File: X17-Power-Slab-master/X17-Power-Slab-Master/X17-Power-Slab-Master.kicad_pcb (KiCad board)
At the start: 2 copper layers, 302.3 x 119 mm, 29 parts, among them J2 ET60T-D04-3-08-D04-X-R1-S, J3 796636-6, Q2 TSM340N06CP ROG

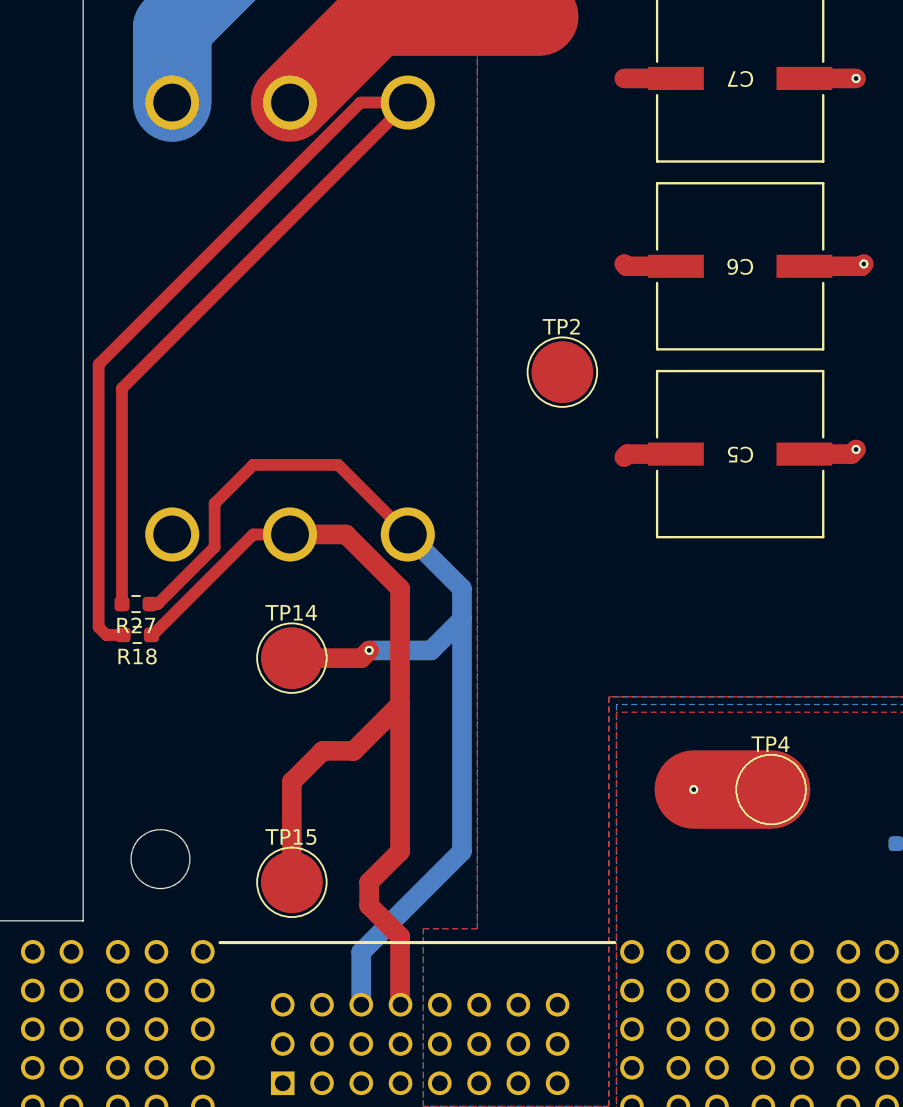
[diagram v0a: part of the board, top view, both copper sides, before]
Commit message: Connector pins renamed and attempt @ fixing airwires for 5V Brick
Still don't understand why the airwire from 5V to 12V_5V_GND test point exists, I also now have airwires across all my P08_1 pins despite the same set up existing for 12V.
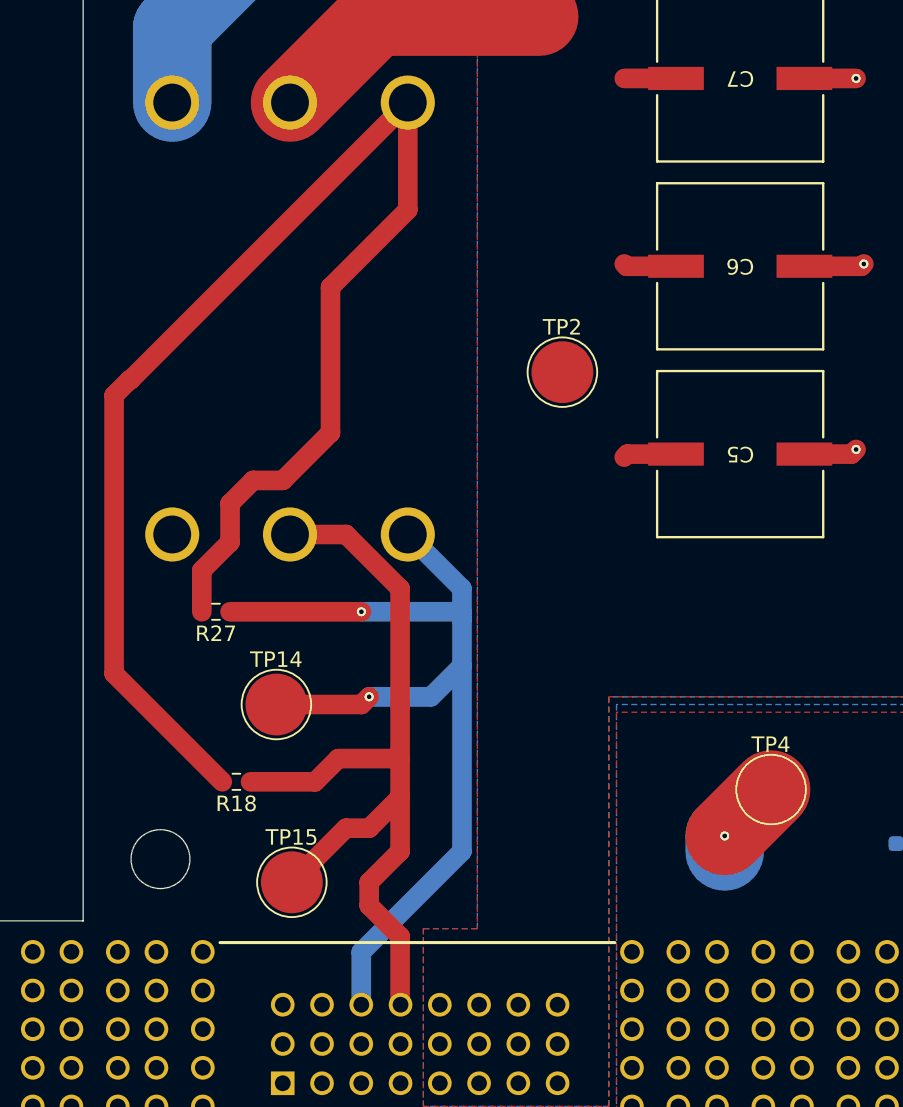
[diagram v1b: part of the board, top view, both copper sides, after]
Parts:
- moved R18 11.5 mm to (81.4, 118.5)
- moved R27 5.19 mm to (80.1, 107.5)
- moved TP14 3.16 mm to (84.0, 113.5)
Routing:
- net Net-(U5-Trim): track 85.9 -> 94.3 mm
- net 5V: track 71.0 -> 63.1 mm, vias 1 -> 2
- net 12V_5V_GND: track 69.4 -> 62.0 mm

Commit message: Minor Edits
Some layout edits, got rid of stm, not done yet
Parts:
- removed the H1 at (-129.8, 147.6)
- removed the H3 at (-7.44, 147.6)
- removed the H4 at (-8.83, 37.2)
- removed TP1, TP4: TestPoint, TestPoint:TestPoint_Pad_D4.0mm
- moved R18 37.1 mm to (89.4, 82.3), turned to 90 degrees
- moved TP2 32.3 mm to (100.6, 124.2)
- moved R27 28.1 mm to (92.5, 82.3), turned to 90 degrees
- moved TP3 7.91 mm to (152.0, 138.0)
- moved TP14 4.61 mm to (88.2, 111.5)
- moved TP15 3.16 mm to (88.0, 124.0), turned to 180 degrees
- moved TP6 2.32 mm to (110.8, 59.5)
- moved R1 1.91 mm to (126.0, 55.0), turned to 180 degrees
- moved TP5 1.80 mm to (77.0, 58.0)
- moved R10 0.75 mm to (125.0, 123.2)
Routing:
- net Net-(U5-Trim): track 94.3 -> 9.93 mm
- net 48V: track 65.5 -> 24.3 mm
- net 12V_5V_GND: track 62.0 -> 25.2 mm
- net RAW_48V_GND: track 30.1 -> 9.58 mm
- net 48V_GND: track 46.1 -> 49.8 mm
- net Net-(U8-SA0/SA1): track 20.2 -> 21.9 mm
- net 5V: track 63.1 -> 63.0 mm, vias 2 -> 0
- added copper zone on F.Cu, net RAW_48V_GND
- removed copper zone on B.Cu, net 48V_GND
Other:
- board size 302.3 x 119 mm -> 129.5 x 99 mm

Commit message: final for 12/30 meeting
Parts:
- removed R18, R27: 10k, Resistor_SMD:R_0603_1608Metric_Pad0.98x0.95mm_HandSolder
- added D2: 48V, Red LED:WL-SMCW_0805, F.Cu at (154.0, 48.0)
- added D3: 12V, Red LED:WL-SMCW_0805, F.Cu at (152.0, 125.0)
- added D4: 5V, Red LED:WL-SMCW_0805, F.Cu at (79.0, 116.0)
- added D5: D_TVS, Diode_SMD:D_SMB_Handsoldering, F.Cu at (149.0, 130.0)
- added R2: 3k, Resistor_SMD:R_0603_1608Metric_Pad0.98x0.95mm_HandSolder, F.Cu at (149.0, 48.0)
- added R3: 250, Resistor_SMD:R_0603_1608Metric_Pad0.98x0.95mm_HandSolder, F.Cu at (145.9, 125.0)
- added R4: 150, Resistor_SMD:R_0603_1608Metric_Pad0.98x0.95mm_HandSolder, F.Cu at (73.9, 116.0)
- added R5: 402k, Resistor_SMD:R_0603_1608Metric_Pad0.98x0.95mm_HandSolder, F.Cu at (81.0, 93.0)
- D1: footprint Diode_SMD:D_1210_3225Metric_Pad1.42x2.65mm_HandSolder -> Diode_SMD:D_MiniMELF
- moved TP15 14.6 mm to (92.0, 110.0)
- moved TP14 11.3 mm to (77.0, 110.0)
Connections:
- J2 pad 06: unconnected-(J2-Pad06) -> (no net)
- J2 pad 08: unconnected-(J2-Pad08) -> 48V_GND
- J2 pad 12: unconnected-(J2-Pad12) -> 12V_5V_GND
- J2 pad 13: unconnected-(J2-Pad13) -> 48V
- J2 pad 14: unconnected-(J2-Pad14) -> 48V
- J2 pad 16: unconnected-(J2-Pad16) -> 48V_GND
- J2 pad 23: 48V_GND -> (no net)
- U5 pad 2: 48V_GND -> unconnected-(U5-RC-Pad2)
- U5 pad 3: Net-(U5-Trim) -> 48V_GND
- U5 pad 4: 5V -> 12V_5V_GND
- U5 pad 5: 12V_5V_GND -> Net-(U5-Vadj)
- U5 pad 6: (no net) -> 5V
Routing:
- net Net-(U5-Vadj): track 0.00 -> 11.2 mm
- net Net-(U5-Trim): track 9.93 -> 0.00 mm
- net 48V_GND: track 49.8 -> 41.2 mm
- net 48V: track 24.3 -> 29.4 mm, vias 5 -> 6
- net Net-(D3-Pad2): track 0.00 -> 4.17 mm
- net Net-(D4-Pad2): track 0.00 -> 3.12 mm
- net Net-(D2-Pad2): track 0.00 -> 3.04 mm
- net 5V: track 63.0 -> 61.4 mm
- net 12V_5V_GND: track 25.2 -> 24.2 mm, vias 1 -> 3

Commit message: Board review 12/30
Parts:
- moved D5 1.30 mm to (150.3, 129.9)
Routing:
- net 48V_GND: track 41.2 -> 28.5 mm
- net 5V: track 61.4 -> 58.1 mm
- net 12V_5V_GND: track 24.2 -> 22.3 mm
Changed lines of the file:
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@@
 	(footprint "Diode_SMD:D_SMB_Handsoldering"
 		(layer "F.Cu")
-		(at 149 130)
+		(at 150.3 129.9)
 		(descr "Diode SMB (DO-214AA) Handsoldering")
 		(tags "Diode SMB (DO-214AA) Handsoldering")
@@
 		(tags "resistor handsolder")
 		(property "Reference" "R5"
-			(at 0 -1.43 360)
+			(at 0 -1.43 0)
 			(layer "F.SilkS")
 			(effects
@@
 		)
 		(property "Value" "402k"
-			(at 0 1.43 360)
+			(at 0 1.43 0)
 			(layer "F.Fab")
 			(effects
@@
 		)
 		(fp_text user "${REFERENCE}"
-			(at 0 0 360)
+			(at 0 0 0)
 			(layer "F.Fab")
 			(effects
@@
 		(descr "<B>WL-SMCW SMT Mono-color Chip LED Waterclear<Br><Br></B>Size: 0805, SMT, 2pins<Br>2x1.25x0.7mm(LXWXH)")
 		(property "Reference" "D2"
-			(at 0 -1.6064 360)
+			(at 0 -1.6064 0)
 			(layer "F.SilkS")
 			(effects
@@
 		)
 		(property "Value" "48V"
-			(at -3 0 360)
+			(at -3 0 0)
 			(layer "F.Fab")
 			(effects
@@
 		)
 		(property "Footprint" "Red LED:WL-SMCW_0805"
-			(at 0 0 360)
+			(at 0 0 0)
 			(layer "F.Fab")
 			(hide yes)
@@
 		)
 		(property "Datasheet" ""
-			(at 0 0 360)
+			(at 0 0 0)
 			(layer "F.Fab")
 			(hide yes)
@@
 		)
 		(property "Description" ""
-			(at 0 0 360)
+			(at 0 0 0)
 			(layer "F.Fab")
 			(hide yes)
@@
 		)
 		(fp_text user "+"
-			(at 1.9 0.3 360)
+			(at 1.9 0.3 0)
 			(layer "F.SilkS")
 			(effects
@@
 		)
 		(fp_text user "+"
-			(at 1.9 0.3 360)
+			(at 1.9 0.3 0)
 			(layer "F.Fab")
 			(effects
@@
 		(tags "resistor handsolder")
 		(property "Reference" "R4"
-			(at 0 -1.43 360)
+			(at 0 -1.43 0)
 			(layer "F.SilkS")
 			(effects
@@
 		)
 		(property "Value" "150"
-			(at 0 1.43 360)
+			(at 0 1.43 0)
 			(layer "F.Fab")
 			(effects
@@
 		)
 		(fp_text user "${REFERENCE}"
-			(at 0 0 360)
+			(at 0 0 0)
 			(layer "F.Fab")
 			(effects
@@
 		(sheetname "Root")
 		(sheetfile "X17-Power-Slab-Master.kicad_sch")
+		(zone_connect 2)
 		(attr smd)
 		(fp_line
@@
 		(sheetname "Root")
 		(sheetfile "X17-Power-Slab-Master.kicad_sch")
+		(zone_connect 2)
 		(attr smd)
 		(fp_line
@@
 		(sheetname "Root")
 		(sheetfile "X17-Power-Slab-Master.kicad_sch")
+		(zone_connect 2)
 		(attr through_hole)
 		(fp_circle
@@
 		(descr "<B>WL-SMCW SMT Mono-color Chip LED Waterclear<Br><Br></B>Size: 0805, SMT, 2pins<Br>2x1.25x0.7mm(LXWXH)")
 		(property "Reference" "D4"
-			(at 0 -1.6064 360)
+			(at 0 -1.6064 0)
 			(layer "F.SilkS")
 			(effects
@@
 		)
 		(property "Value" "5V"
-			(at -3 0 360)
+			(at -3 0 0)
 			(layer "F.Fab")
 			(effects
@@
 		)
 		(property "Footprint" "Red LED:WL-SMCW_0805"
-			(at 0 0 360)
+			(at 0 0 0)
 			(layer "F.Fab")
 			(hide yes)
@@
 		)
 		(property "Datasheet" ""
-			(at 0 0 360)
+			(at 0 0 0)
 			(layer "F.Fab")
 			(hide yes)
@@
 		)
 		(property "Description" ""
-			(at 0 0 360)
+			(at 0 0 0)
 			(layer "F.Fab")
 			(hide yes)
@@
 		)
 		(fp_text user "+"
-			(at 1.9 0.3 360)
+			(at 1.9 0.3 0)
 			(layer "F.SilkS")
 			(effects
@@
 		)
 		(fp_text user "+"
-			(at 1.9 0.3 360)
+			(at 1.9 0.3 0)
 			(layer "F.Fab")
 			(effects
@@
 		)
 		(property "Value" "12V"
-			(at -2.95 0 360)
+			(at -2.95 0 0)
 			(layer "F.Fab")
 			(effects
@@
 		)
 		(property "Footprint" "Red LED:WL-SMCW_0805"
-			(at 0 0 360)
+			(at 0 0 0)
 			(layer "F.Fab")
 			(hide yes)
@@
 		)
 		(property "Datasheet" ""
-			(at 0 0 360)
+			(at 0 0 0)
 			(layer "F.Fab")
 			(hide yes)
@@
 		)
 		(property "Description" ""
-			(at 0 0 360)
+			(at 0 0 0)
 			(layer "F.Fab")
 			(hide yes)
@@
 		)
 		(fp_text user "+"
-			(at 1.9 0.3 360)
+			(at 1.9 0.3 0)
 			(layer "F.SilkS")
 			(effects
@@
 		)
 		(fp_text user "+"
-			(at 1.9 0.3 360)
+			(at 1.9 0.3 0)
 			(layer "F.Fab")
 			(effects
@@
 		(sheetname "Root")
 		(sheetfile "X17-Power-Slab-Master.kicad_sch")
+		(zone_connect 2)
 		(attr smd)
 		(fp_line
@@
 		(sheetname "48Vto5V")
 		(sheetfile "untitled.kicad_sch")
+		(zone_connect 2)
 		(attr through_hole)
 		(fp_rect
@@
 		(sheetname "Root")
 		(sheetfile "X17-Power-Slab-Master.kicad_sch")
+		(zone_connect 2)
 		(attr through_hole)
 		(fp_rect
@@
 	)
 	(segment
-		(start 72.95 116)
-		(end 72.95 114.05)
+		(start 77.2 109.8)
+		(end 77.2 102.56)
 		(width 1.27)
 		(layer "F.Cu")
@@
 	(segment
 		(start 89.49 132.92)
-		(end 89.49 116.49)
+		(end 89.5 132.91)
+		(width 1.27)
+		(layer "F.Cu")
+		(net 2)
+	)
+	(segment
+		(start 77.2 102.56)
+		(end 77.26 102.5)
+		(width 1.27)
+		(layer "F.Cu")
+		(net 2)
+	)
+	(segment
+		(start 72.95 116)
+		(end 72.95 114.05)
 		(width 1.27)
 		(layer "F.Cu")
@@
 	)
 	(segment
-		(start 77.26 104.26)
-		(end 77.26 102.5)
+		(start 77 110)
+		(end 77.2 109.8)
 		(width 1.27)
 		(layer "F.Cu")
@@
 	)
 	(segment
-		(start 89.49 116.49)
-		(end 77.26 104.26)
+		(start 89.5 132.91)
+		(end 89.5 117.1)
 		(width 1.27)
 		(layer "F.Cu")
@@
 	)
 	(segment
-		(start 77 110)
-		(end 77 102.76)
+		(start 82.4 110)
+		(end 89.5 117.1)
 		(width 1.27)
 		(layer "F.Cu")
@@
 	)
 	(segment
-		(start 80.0875 99.6725)
+		(start 78.1 102.5)
 		(end 77.26 102.5)
 		(width 1.27)
@@
 	)
 	(segment
-		(start 77 102.76)
+		(start 80.0875 99.6725)
 		(end 77.26 102.5)
 		(width 1.27)
@@
 	)
 	(segment
+		(start 77 110)
+		(end 82.4 110)
+		(width 1.27)
+		(layer "F.Cu")
+		(net 2)
+	)
+	(segment
 		(start 155.05 58.95)
 		(end 155 59)
@@
 	)
 	(segment
-		(start 105.8006 85.1506)
-		(end 105.8 85.15)
-		(width 1.524)
-		(layer "F.Cu")
-		(net 3)
-	)
-	(segment
-		(start 109.8471 97.3012)
-		(end 106.0012 97.3012)
-		(width 1.524)
-		(layer "F.Cu")
-		(net 3)
-	)
-	(segment
 		(start 133.0125 58.4875)
 		(end 131.5 58.4875)
@@
 	)
 	(segment
-		(start 109.8471 73)
-		(end 105 73)
-		(width 1.524)
-		(layer "F.Cu")
-		(net 3)
-	)
-	(segment
 		(start 134 57.5)
 		(end 133.0125 58.4875)
@@
 	)
 	(segment
-		(start 109.8471 85.1506)
-		(end 105.8006 85.1506)
-		(width 1.524)
-		(layer "F.Cu")
-		(net 3)
-	)
-	(segment
 		(start 134 54.638)
 		(end 134 57.5)
@@
 	)
 	(segment
-		(start 106.0012 97.3012)
-		(end 106 97.3)
-		(width 1.524)
-		(layer "F.Cu")
-		(net 3)
-	)
-	(segment
 		(start 125.17 47.715)
 		(end 127.077 47.715)
@@
 	)
 	(segment
-		(start 153.05 128.65)
-		(end 153.05 125)
-		(width 1.524)
-		(layer "F.Cu")
-		(net 19)
-	)
-	(segment
-		(start 151.7 130)
-		(end 157 130)
-		(width 1.524)
-		(layer "F.Cu")
-		(net 19)
-	)
-	(segment
 		(start 92 132.89)
 		(end 92.03 132.92)
@@
 	)
 	(segment
-		(start 151.7 130)
-		(end 153.05 128.65)
+		(start 157 129.9)
+		(end 153 129.9)
+		(width 1.524)
+		(layer "F.Cu")
+		(net 19)
+	)
+	(segment
+		(start 153.05 129.85)
+		(end 153.05 125)
 		(width 1.524)
 		(layer "F.Cu")
@@
 	)
 	(segment
+		(start 153 129.9)
+		(end 153.05 129.85)
+		(width 1.524)
+		(layer "F.Cu")
+		(net 19)
+	)
+	(segment
 		(start 85 118)
 		(end 83 116)
@@
 	)
 	(via
-		(at 157 130)
+		(at 157 129.9)
 		(size 1.27)
 		(drill 0.762)
@@
 		(hatch edge 0.5)
 		(priority 4)
-		(connect_pads
+		(connect_pads yes
 			(clearance 0.508)
 		)
@@
 		(hatch edge 0.5)
 		(priority 7)
-		(connect_pads
+		(connect_pads yes
 			(clearance 0.508)
 		)
@@
 		(polygon
 			(pts
-				(xy 82 100) (xy 96 100) (xy 96 137) (xy 106 137) (xy 106 113.6) (xy 163 113.6) (xy 163 142) (xy 82 142)
+				(xy 71.9 88.5) (xy 96 88.6) (xy 96 137) (xy 106 137) (xy 106 113.6) (xy 163 113.6) (xy 163 142)
+				(xy 71.9 141.9)
 			)
 		)

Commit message: changes 1/3/25
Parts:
- added J1: Conn_01x12_Pin, DataConv Connector:Data Conversion two 1x6, F.Cu at (118.1, 97.3)
- moved C5 47.8 mm to (133.9, 53.9)
- moved C6 27.3 mm to (141.3, 85.7)
- moved C7 27.3 mm to (141.3, 73.6)
- moved TP15 24.8 mm to (75.0, 92.0), turned to 0 degrees
- moved D1 21.7 mm to (111.0, 64.0)
- moved R1 11.4 mm to (118.0, 63.1), turned to 90 degrees
- moved TP6 9.76 mm to (101.0, 60.0)
- moved R5 5.10 mm to (82.0, 98.0)
- moved Q2 4.97 mm to (119.7, 54.8), turned to 90 degrees
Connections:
- U8 pad 9: C2 -> PG
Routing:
- net PG: track 0.00 -> 68.0 mm
- net 5V: track 58.1 -> 114.7 mm, vias 0 -> 1
- net A-: track 0.00 -> 55.4 mm
- net A+: track 0.00 -> 54.5 mm
- net 12V_5V_GND: track 22.3 -> 76.4 mm
- net ALERT1: track 0.00 -> 53.0 mm
- net DATA: track 0.00 -> 51.4 mm
- net NRST_PSB: track 0.00 -> 48.3 mm, vias 0 -> 1
- net SWCLK: track 0.00 -> 30.8 mm
- net 48V_GND: track 28.5 -> 0.00 mm
- net Net-(U5-Vadj): track 11.2 -> 5.31 mm
- net RAW_48V_GND: track 9.58 -> 12.7 mm
- net 48V: track 29.4 -> 30.7 mm
- net Net-(D1-K): track 11.3 -> 10.4 mm

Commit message: changes 1/9/25 AMs
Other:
- board text added: "1"
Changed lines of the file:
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@@
 		(tags "Diode SMB (DO-214AA) Handsoldering")
 		(property "Reference" "D5"
-			(at 0 -3 0)
+			(at -5.96 2.67 0)
 			(layer "F.SilkS")
 			(effects
 				(font
 					(size 1 1)
-					(thickness 0.15)
+					(thickness 0.1524)
 				)
 			)
@@
 				(font
 					(size 1 1)
-					(thickness 0.15)
+					(thickness 0.1524)
 				)
 			)
@@
 				(font
 					(size 1 1)
-					(thickness 0.15)
+					(thickness 0.1524)
 				)
 			)
@@
 				(font
 					(size 1 1)
-					(thickness 0.15)
+					(thickness 0.1524)
 				)
 			)
@@
 				(font
 					(size 1 1)
-					(thickness 0.15)
+					(thickness 0.1524)
 				)
 			)
@@
 				(font
 					(size 1 1)
-					(thickness 0.15)
+					(thickness 0.1524)
 				)
 			)
@@
 		(at 118.085 97.315 -90)
 		(property "Reference" "J1"
-			(at 0 -0.5 -90)
+			(at -1.965 -3.065 -90)
 			(unlocked yes)
 			(layer "F.SilkS")
@@
 				(font
 					(size 1 1)
-					(thickness 0.1)
+					(thickness 0.1524)
 				)
 			)
@@
 		(attr smd)
 		(fp_line
+			(start 19.275 5.995)
+			(end -18.15 5.995)
+			(stroke
+				(width 0.1)
+				(type default)
+			)
+			(layer "F.SilkS")
+		)
+		(fp_line
 			(start -19.48 5.525)
 			(end -16.82 5.525)
@@
 			(layer "F.SilkS")
 		)
-		(fp_rect
+		(fp_line
 			(start -18.15 -10.25)
-			(end 19.275 5.925)
+			(end 19.275 -10.25)
 			(stroke
 				(width 0.1)
 				(type default)
 			)
-			(fill none)
 			(layer "F.SilkS")
 		)
@@
 		)
 		(fp_text user "${REFERENCE}"
-			(at -18.15 -2.155 360)
+			(at -18.15 -2.155 0)
 			(layer "F.Fab")
 			(effects
@@
 		)
 		(fp_text user "${REFERENCE}"
-			(at 15.575 -4.895 360)
+			(at 15.575 -4.895 0)
 			(layer "F.Fab")
 			(effects
@@
 		(descr "<B>WL-SMCW SMT Mono-color Chip LED Waterclear<Br><Br></B>Size: 0805, SMT, 2pins<Br>2x1.25x0.7mm(LXWXH)")
 		(property "Reference" "D2"
-			(at 0 -1.6064 0)
+			(at 0.04 -1.84 0)
 			(layer "F.SilkS")
 			(effects
 				(font
-					(size 0.64 0.64)
-					(thickness 0.15)
+					(size 1.016 1.016)
+					(thickness 0.1524)
 				)
 			)
@@
 		)
 		(fp_text user "+"
-			(at 1.9 0.3 0)
+			(at 2.24 -1.39 0)
 			(layer "F.SilkS")
 			(effects
 				(font
-					(size 0.48 0.48)
-					(thickness 0.15)
-				)
-			)
-		)
-		(fp_text user "+"
-			(at 1.9 0.3 0)
-			(layer "F.Fab")
-			(effects
-				(font
-					(size 0.48 0.48)
-					(thickness 0.15)
+					(size 1.016 1.016)
+					(thickness 0.1524)
 				)
 			)
@@
 				(font
 					(size 1 1)
-					(thickness 0.15)
+					(thickness 0.1524)
 				)
 			)
@@
 				(font
 					(size 1 1)
-					(thickness 0.15)
+					(thickness 0.1524)
 				)
 			)
@@
 				(font
 					(size 1 1)
-					(thickness 0.15)
+					(thickness 0.1524)
 				)
 			)
@@
 				(font
 					(size 1 1)
-					(thickness 0.15)
+					(thickness 0.1524)
 				)
 			)
@@
 				(font
 					(size 1 1)
-					(thickness 0.15)
+					(thickness 0.1524)
 				)
 			)
@@
 				(font
 					(size 1 1)
-					(thickness 0.15)
+					(thickness 0.1524)
 				)
 			)
@@
 				(font
 					(size 1 1)
-					(thickness 0.15)
+					(thickness 0.1524)
 				)
 			)
@@
 				(font
 					(size 1 1)
-					(thickness 0.15)
+					(thickness 0.1524)
 				)
 			)
@@
 			(at 27.432 0 0)
 			(unlocked yes)
-			(layer "B.SilkS")
-			(effects
-				(font
-					(size 1 1)
-					(thickness 0.15)
-				)
-			)
-		)
-		(fp_text user "6"
-			(at 27.432 0 0)
-			(unlocked yes)
-			(layer "B.SilkS")
-			(effects
-				(font
-					(size 1 1)
-					(thickness 0.15)
-				)
-			)
-		)
-		(fp_text user "1"
-			(at -2.032 0 0)
-			(unlocked yes)
-			(layer "B.SilkS")
-			(effects
-				(font
-					(size 1 1)
-					(thickness 0.15)
-				)
-			)
-		)
-		(fp_text user "1"
-			(at -2.032 0 0)
-			(unlocked yes)
-			(layer "F.SilkS")
-			(effects
-				(font
-					(size 1 1)
-					(thickness 0.15)
-				)
-			)
-		)
-		(fp_text user "6"
-			(at 27.432 0 0)
-			(unlocked yes)
-			(layer "F.SilkS")
-			(effects
-				(font
-					(size 1 1)
-					(thickness 0.15)
-				)
-			)
-		)
-		(fp_text user "6"
-			(at 27.432 0 0)
-			(unlocked yes)
-			(layer "F.SilkS")
-			(effects
-				(font
-					(size 1 1)
-					(thickness 0.15)
-				)
-			)
-		)
-		(fp_text user "1"
-			(at -2.032 0 0)
-			(unlocked yes)
 			(layer "F.SilkS")
 			(effects
 				(font
 					(size 1 1)
-					(thickness 0.15)
+					(thickness 0.1524)
 				)
 			)
@@
 				(font
 					(size 1 1)
-					(thickness 0.15)
+					(thickness 0.1524)
 				)
 			)
@@
 				(font
 					(size 1 1)
-					(thickness 0.15)
+					(thickness 0.1524)
 				)
 			)
@@
 		(descr "<B>WL-SMCW SMT Mono-color Chip LED Waterclear<Br><Br></B>Size: 0805, SMT, 2pins<Br>2x1.25x0.7mm(LXWXH)")
 		(property "Reference" "D4"
-			(at 0 -1.6064 0)
+			(at -0.02 -1.84 0)
 			(layer "F.SilkS")
 			(effects
 				(font
-					(size 0.64 0.64)
-					(thickness 0.15)
+					(size 1.016 1.016)
+					(thickness 0.1524)
 				)
 			)
@@
 		)
 		(fp_text user "+"
-			(at 1.9 0.3 0)
+			(at 2 -1.4 0)
 			(layer "F.SilkS")
 			(effects
 				(font
-					(size 0.48 0.48)
-					(thickness 0.15)
-				)
-			)
-		)
-		(fp_text user "+"
-			(at 1.9 0.3 0)
-			(layer "F.Fab")
-			(effects
-				(font
-					(size 0.48 0.48)
-					(thickness 0.15)
+					(size 1.016 1.016)
+					(thickness 0.1524)
 				)
 			)
@@
 				(font
 					(size 1 1)
-					(thickness 0.15)
+					(thickness 0.1524)
 				)
 			)
@@
 		(descr "<B>WL-SMCW SMT Mono-color Chip LED Waterclear<Br><Br></B>Size: 0805, SMT, 2pins<Br>2x1.25x0.7mm(LXWXH)")
 		(property "Reference" "D3"
-			(at 0 -2 180)
+			(at -0.66 2.24 180)
 			(layer "F.SilkS")
 			(effects
 				(font
-					(size 0.64 0.64)
-					(thickness 0.15)
+					(size 1.016 1.016)
+					(thickness 0.1524)
 				)
 			)
@@
 		)
 		(fp_text user "+"
-			(at 1.9 0.3 0)
-			(layer "F.SilkS")
-			(effects
-				(font
-					(size 0.48 0.48)
-					(thickness 0.15)
-				)
-			)
-		)
-		(fp_text user "+"
-			(at 1.9 0.3 0)
+			(at 1.64 2.14 0)
 			(layer "F.Fab")
 			(effects
 				(font
-					(size 0.48 0.48)
-					(thickness 0.15)
+					(size 1.016 1.016)
+					(thickness 0.1524)
 				)
 			)
@@
 				(font
 					(size 1 1)
-					(thickness 0.15)
+					(thickness 0.1524)
 				)
 			)
@@
 				(font
 					(size 1 1)
-					(thickness 0.15)
+					(thickness 0.1524)
 				)
 			)
@@
 				(font
 					(size 1 1)
-					(thickness 0.1)
+					(thickness 0.1524)
 				)
 				(justify mirror)
@@
 		(at 148.5 90.75 -90)
 		(property "Reference" "U8"
-			(at 0 1.3471 90)
+			(at 2.39 -1.59 90)
 			(unlocked yes)
 			(layer "B.SilkS")
@@
 				(font
 					(size 1 1)
-					(thickness 0.1)
+					(thickness 0.1524)
 				)
 				(justify mirror)
@@
 		(layer "Edge.Cuts")
 	)
+	(gr_text "1"
+		(at 83.41 50.02 0)
+		(layer "F.SilkS")
+		(effects
+			(font
+				(size 1 1)
+				(thickness 0.1524)
+			)
+		)
+	)
 	(segment
